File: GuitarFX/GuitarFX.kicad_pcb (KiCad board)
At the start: 4 copper layers, 70 x 85 mm, 122 parts, among them IC401 PCM3060PWR, J202 Screw_Terminal_01x02, J301 USB_C_Receptacle_USB2.0, J302 Conn_ARM_SWD_TagConnect_TC2030, J303 Screw_Terminal_01x06, J401 Screw_Terminal_01x02, J402 Screw_Terminal_01x02, SW301 SW_SPDT, U201 NCP718xSN500, U202 NCP1117-3.3_SOT223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

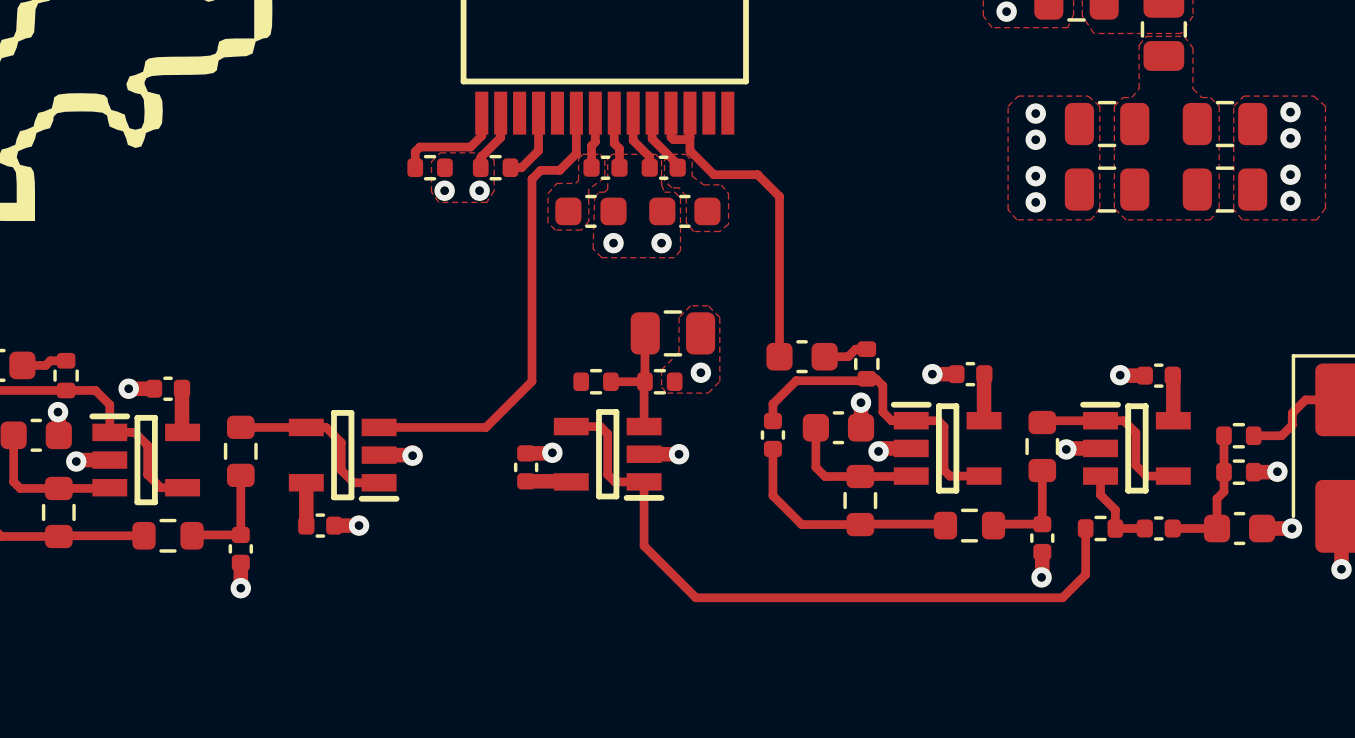
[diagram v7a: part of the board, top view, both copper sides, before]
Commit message: 5VA Power routing complete
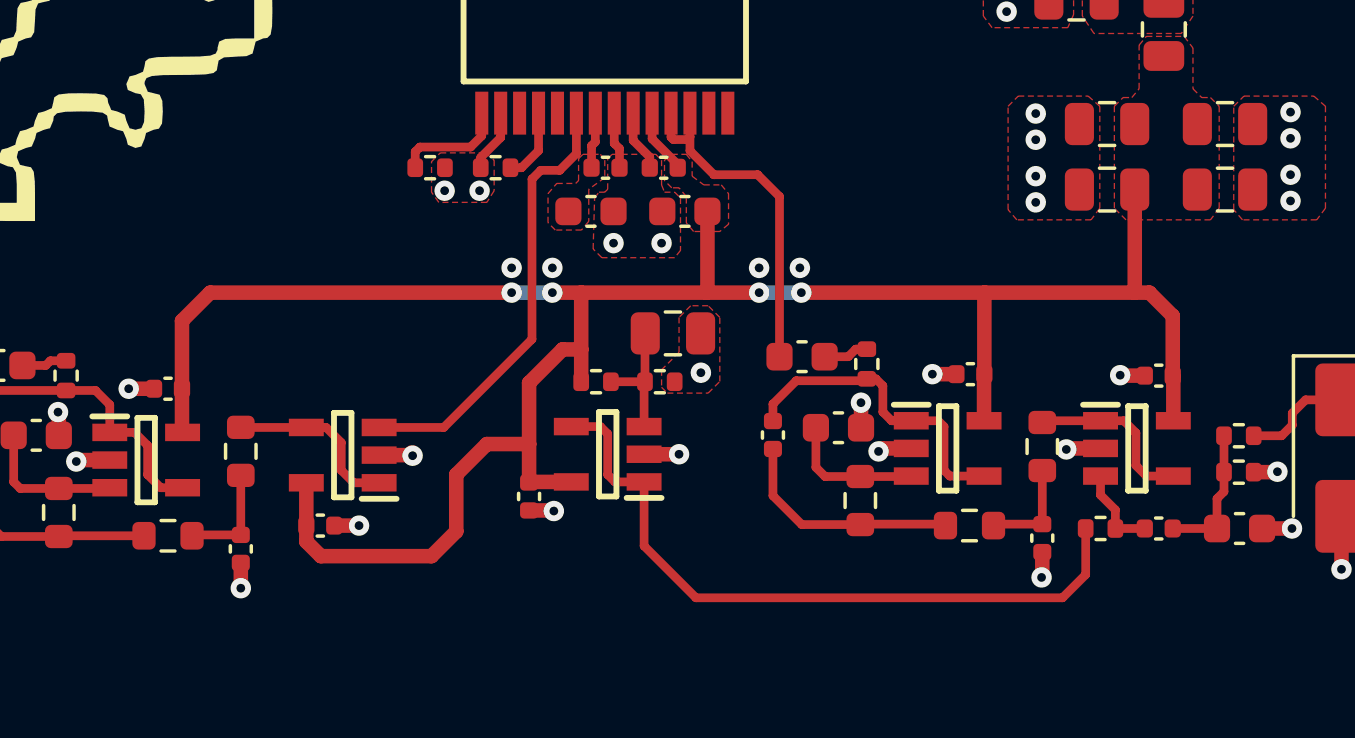
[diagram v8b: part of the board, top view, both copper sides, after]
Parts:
- moved C402 1.00 mm to (142.4, 132.2), turned to -90 degrees
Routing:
- net +5VA: track 9.94 -> 78.0 mm, vias 0 -> 4
- net /Codec/CODEC_VOUT: track 16.1 -> 15.3 mm
- net GND: vias 82 -> 86
